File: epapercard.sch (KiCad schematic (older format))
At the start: 35 parts

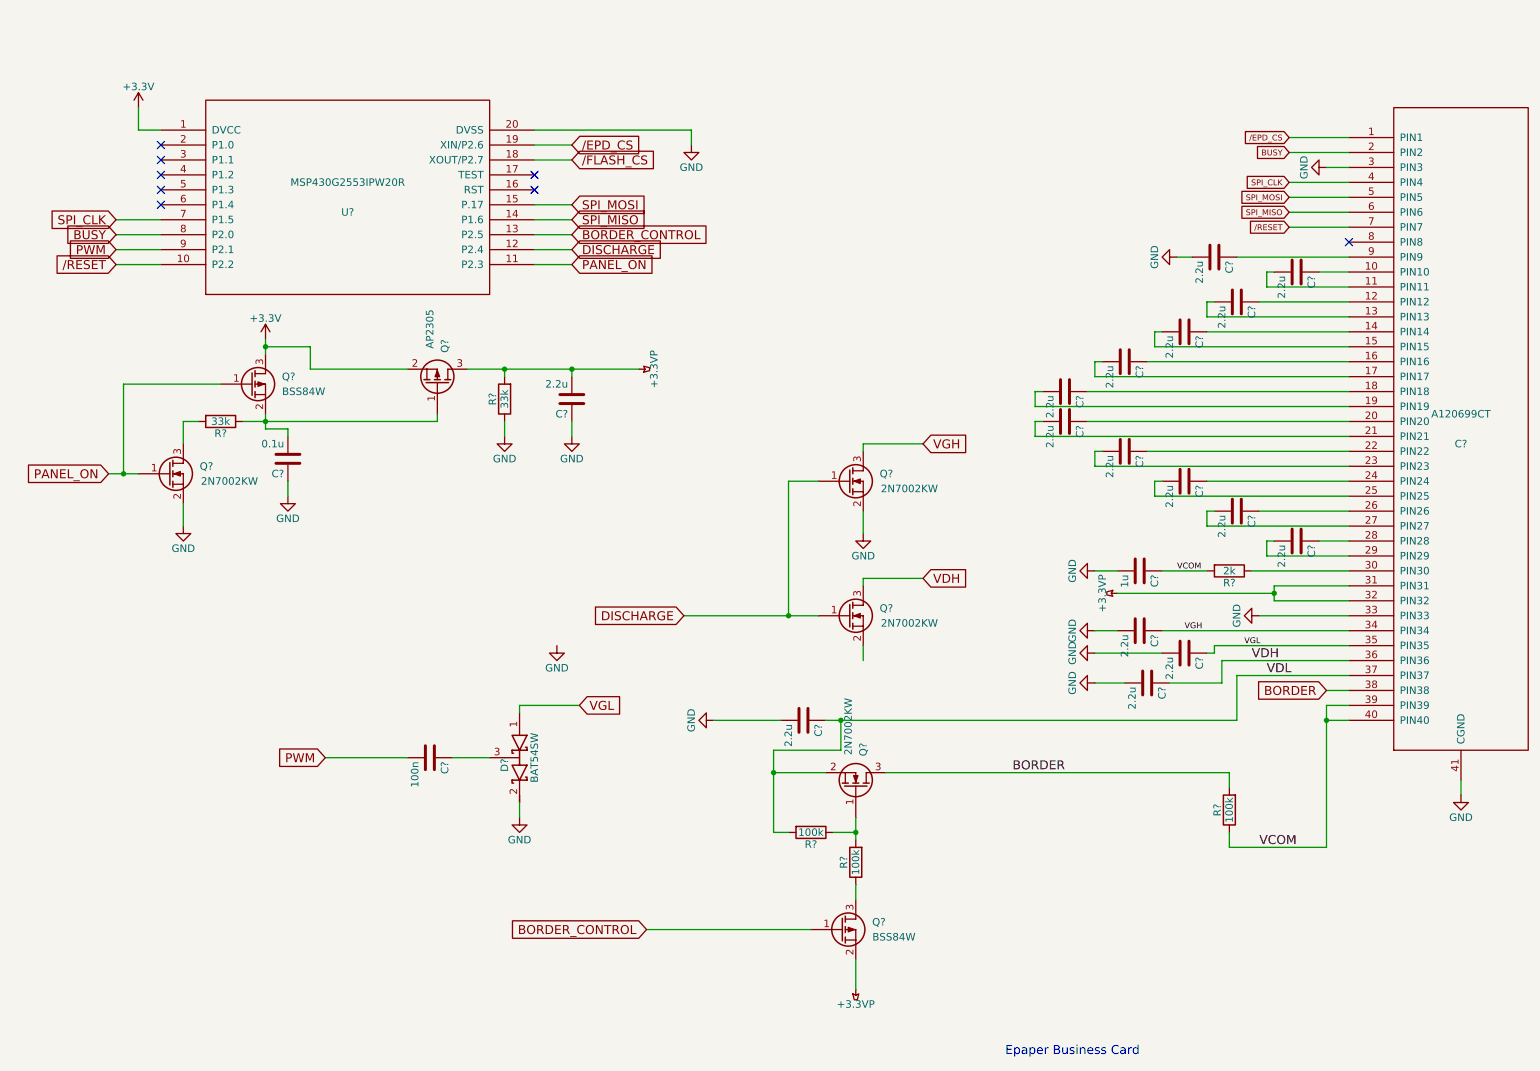
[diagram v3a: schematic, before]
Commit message: Fixed some labels
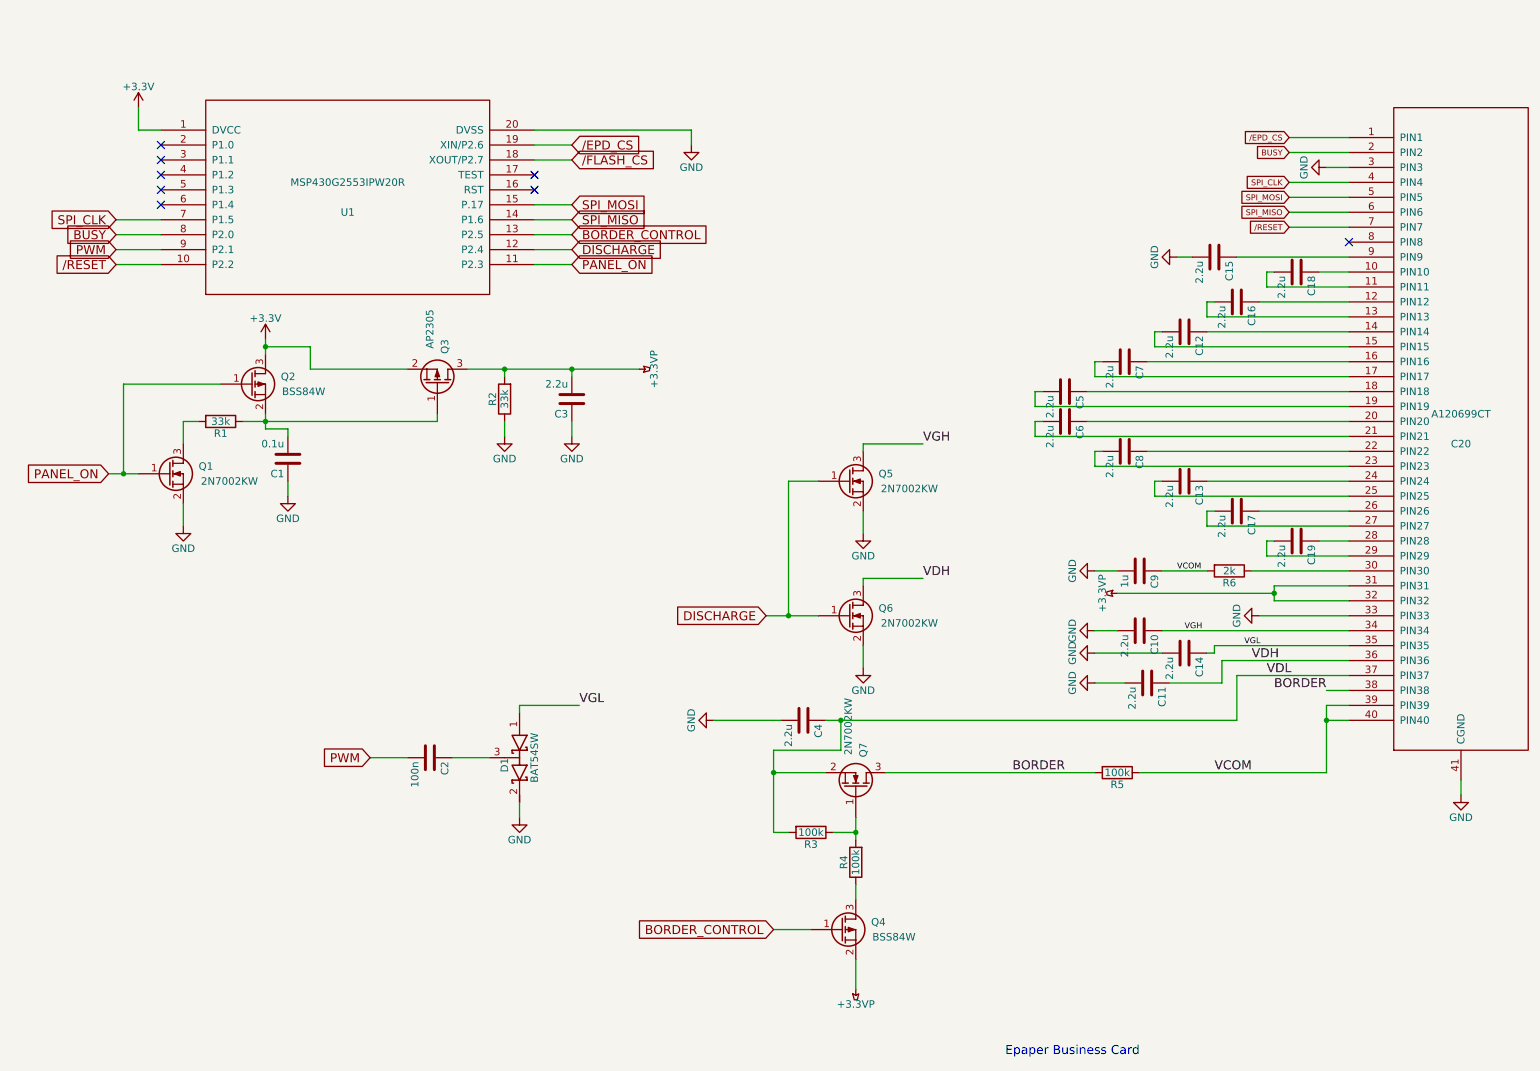
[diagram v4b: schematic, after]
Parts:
- gave numbers to parts that had none: 35
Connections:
- net GND: now also Q6.2 (S)
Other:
- moved on the sheet: R5

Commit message: Added programming circuit
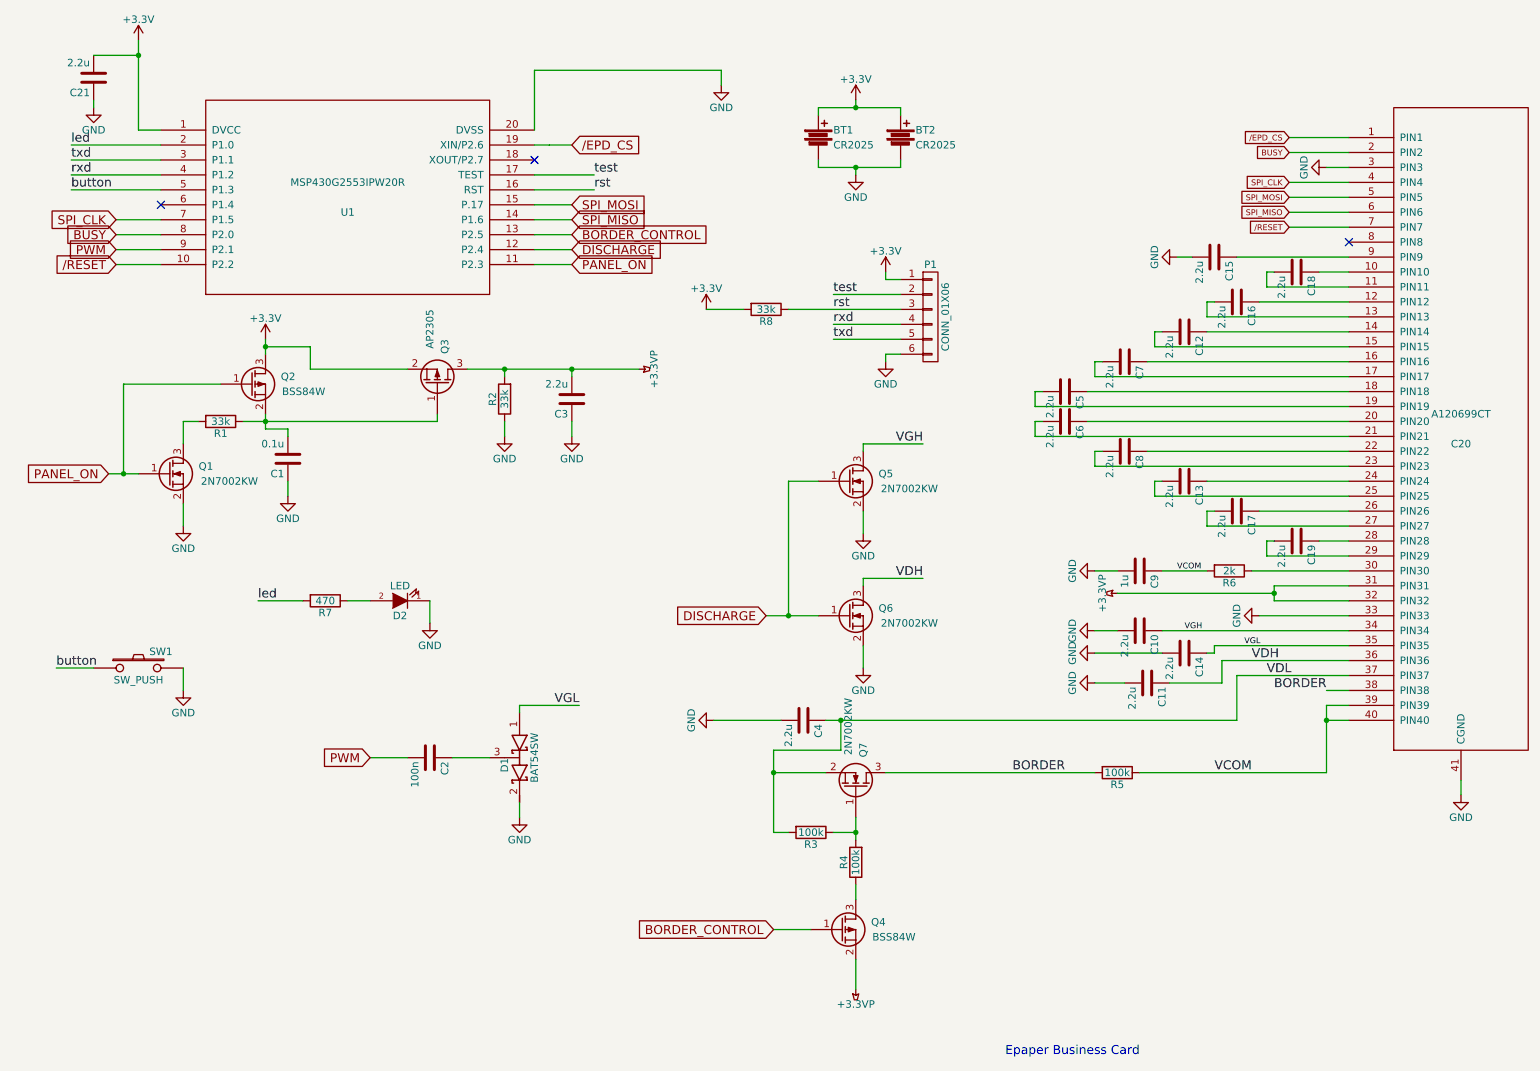
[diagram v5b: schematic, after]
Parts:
- added BT1, BT2: CR2025, symbol Battery
- added C21: 2.2u, symbol C
- added D2: LED, symbol LED
- added P1: CONN_01X06, symbol CONN_01X06
- added R7: 470, symbol R
- added R8: 33k, symbol R
- added SW1: SW_PUSH, symbol SW_PUSH
- C20: footprint MODULE -> footprint:A120699CT
- U1: footprint MODULE -> Housings_SSOP:TSSOP-20_4.4x6.5mm_Pitch0.65mm
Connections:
- net +3V3: now also BT1.1, BT2.1, C21.2, P1.1 (P1), R8.2
- net GND: now also BT1.2, BT2.2, C21.1, D2.1 (K), P1.6 (P6), SW1.2
- net rst: now reaches U1.16 (RST)
- net rst: now also P1.3 (P3), R8.1
- net test: now reaches U1.17 (TEST)
- net test: now also P1.2 (P2)
- net led: now reaches U1.2 (P1.0)
- net led: now also R7.2
- net txd: now reaches U1.3 (P1.1)
- net txd: now also P1.5 (P5)
- net rxd: now reaches U1.4 (P1.2)
- net rxd: now also P1.4 (P4)
- net button: now reaches U1.5 (P1.3)
- net button: now also SW1.1
- net /FLASH_CS: no longer names the net of U1.18 (XOUT/P2.7)
- new net: D2.2 (A), R7.1
- no-connect marks 8 -> 3

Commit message: Attached footprints
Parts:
- BT1, BT2: value CR2025 -> CR2032; footprint (none) -> footprint:CR2032
- C1, C10, C11, C12, C13, C14, C15, C16, C17, C18, C19, C2, C21, C3, C4, C5, C6, C7, C8, C9, D2: footprint (none) -> Capacitors_SMD:C_0805_HandSoldering
- D1, Q1, Q2, Q3, Q4, Q5, Q6, Q7: footprint (none) -> TO_SOT_Packages_SMD:SOT-323
- P1: footprint (none) -> Pin_Headers:Pin_Header_Straight_1x06
- R1, R2, R3, R4, R5, R6, R7, R8: footprint (none) -> Resistors_SMD:R_0805_HandSoldering
- SW1: footprint (none) -> Buttons_Switches_SMD:SW_SPST_EVPBF
- renumbered C20 to P2

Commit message: Laying board out
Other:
- note removed: "Epaper Business Card"
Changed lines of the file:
@@
 encoding utf-8
 Sheet 1 1
-Title ""
+Title "Epaper Business Card"
 Date ""
 Rev ""
-Comp ""
+Comp "paulschow.com"
 Comment1 ""
 Comment2 ""
@@
 Wire Wire Line
 	9650 5050 9500 5050
-Text Notes 7350 7500 0    60   ~ 0
-Epaper Business Card
 $Comp
 L Q_NMOS_GSD Q5

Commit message: Switched to surface mount battery holders
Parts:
- BT1, BT2: footprint footprint:CR2032 -> footprint:CR2032sm
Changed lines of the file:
@@
 F 0 "BT1" H 6200 1400 50  0000 L CNN
 F 1 "CR2032" H 6200 1300 50  0000 L CNN
-F 2 "footprint:CR2032" V 6100 1390 50  0001 C CNN
+F 2 "footprint:CR2032sm" V 6100 1390 50  0001 C CNN
 F 3 "" V 6100 1390 50  0000 C CNN
 	1    6100 1350
@@
 F 0 "BT2" H 6750 1400 50  0000 L CNN
 F 1 "CR2032" H 6750 1300 50  0000 L CNN
-F 2 "footprint:CR2032" V 6650 1390 50  0001 C CNN
+F 2 "footprint:CR2032sm" V 6650 1390 50  0001 C CNN
 F 3 "" V 6650 1390 50  0000 C CNN
 	1    6650 1350
